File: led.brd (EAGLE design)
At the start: 60.9 x 55.9 mm, 12 parts

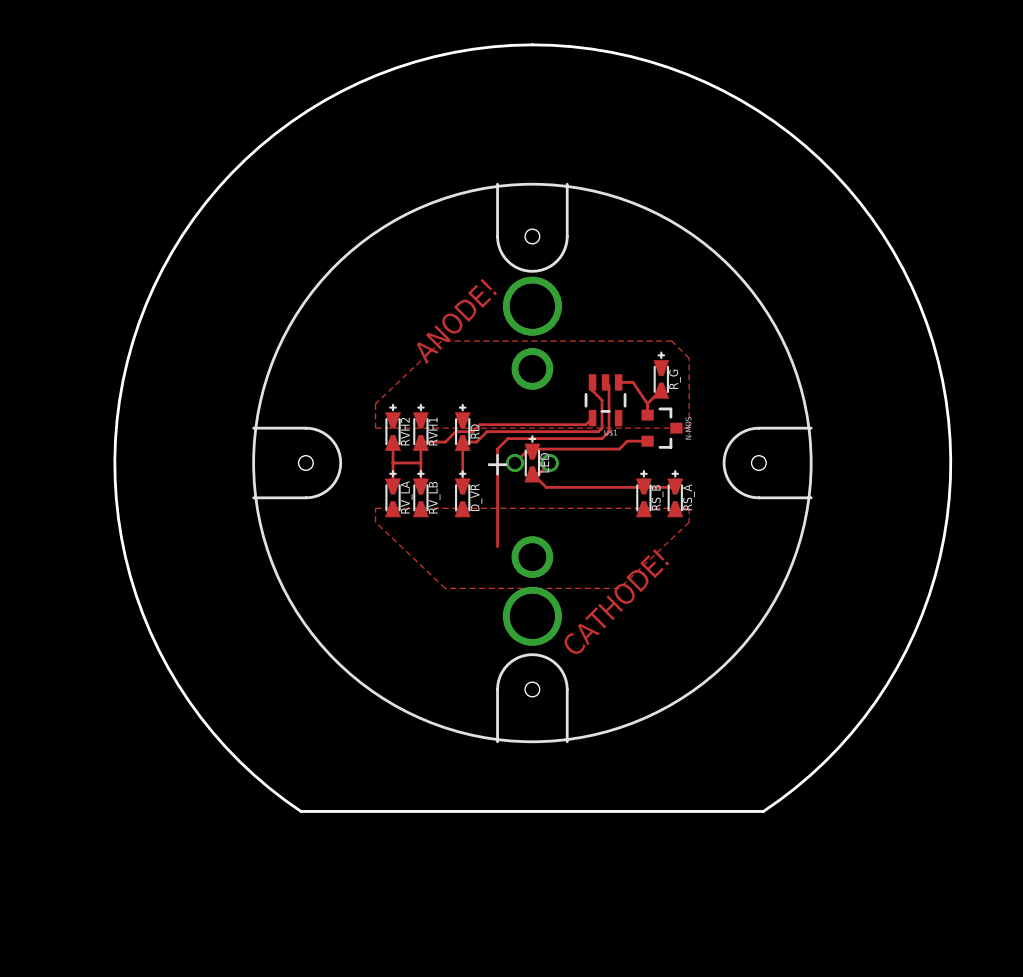
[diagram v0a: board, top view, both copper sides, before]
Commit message: correct LED circuit
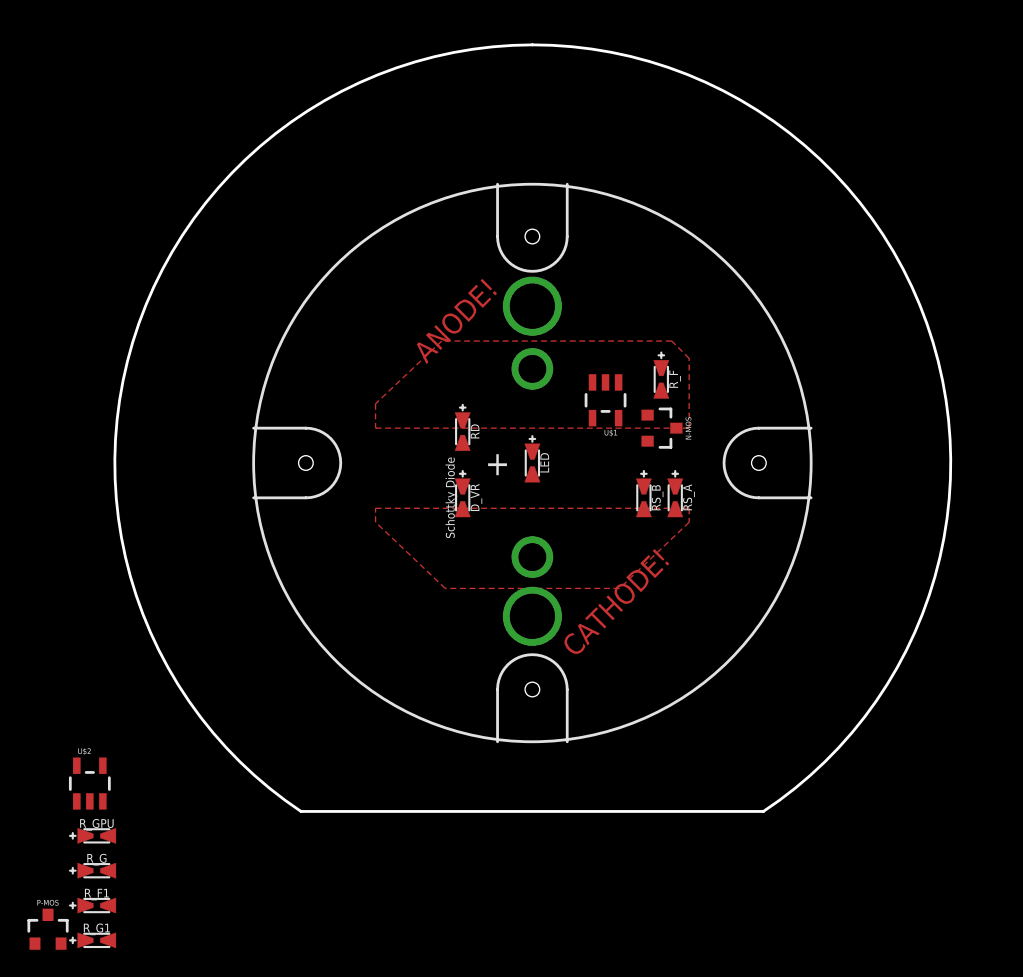
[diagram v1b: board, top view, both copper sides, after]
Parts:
- removed RVH1, RVH2, RV_LA, RV_LB: (no value), tekdemo:0402-0603-0805-UNIVERSAL
- added P-MOS: (no value), tekdemo:SOT23-3
- added R_F, R_F1, R_G1, R_GPU: (no value), tekdemo:0402-0603-0805-UNIVERSAL
- added U$2: OPA344, SparkFun-AnalogIC:SOT23-5
- D_VR: value (none) -> Schottky Diode
- moved R_G 54.6 mm to (-1.27, 0.76), turned to 0 degrees
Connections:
- removed net LED+: LED.+, N-MOS.2
- removed net LED-: LED.-, RS_A.+, RS_B.+
- removed net N$7: RVH1.-, RVH2.-, RV_LA.+, RV_LB.+, U$1.4
- removed net N$8: D_VR.+, RD.-, U$1.3
- new net GATE: N-MOS.1, R_GPU.+, U$2.1
- new net N$2: N-MOS.2, RS_A.+, RS_B.+
- new net VCC: LED.+, P-MOS.2, R_GPU.-, U$1.5, U$2.5
- new net VDIV: R_F.+, R_F1.+, R_G.-, R_G1.-, U$1.4
- new net VREF: RD.+, U$2.3
- new net VSENSE: LED.-, N-MOS.3, U$1.3
- new net V_AMP: R_F.-, R_F1.-, U$1.1, U$2.4
- net GND: now also P-MOS.1, R_G.+, R_G1.+, U$2.2; no longer RV_LA.-, RV_LB.-
- net N$3: now also D_VR.+, RD.-; no longer N-MOS.1, R_G.-, U$1.1
- net VIN: now also P-MOS.3; no longer N-MOS.3, RD.+, RVH1.+, RVH2.+, R_G.+, U$1.5
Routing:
- net N$7: track 21.9 -> 0.00 mm
- net GND: track 19.5 -> 0.00 mm
- net N$8: track 17.5 -> 0.00 mm
- net LED-: track 12.4 -> 0.00 mm, vias 1 -> 0
- net LED+: track 10.3 -> 0.00 mm, vias 1 -> 0
- net N$3: track 6.02 -> 0.00 mm

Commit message: routed led board
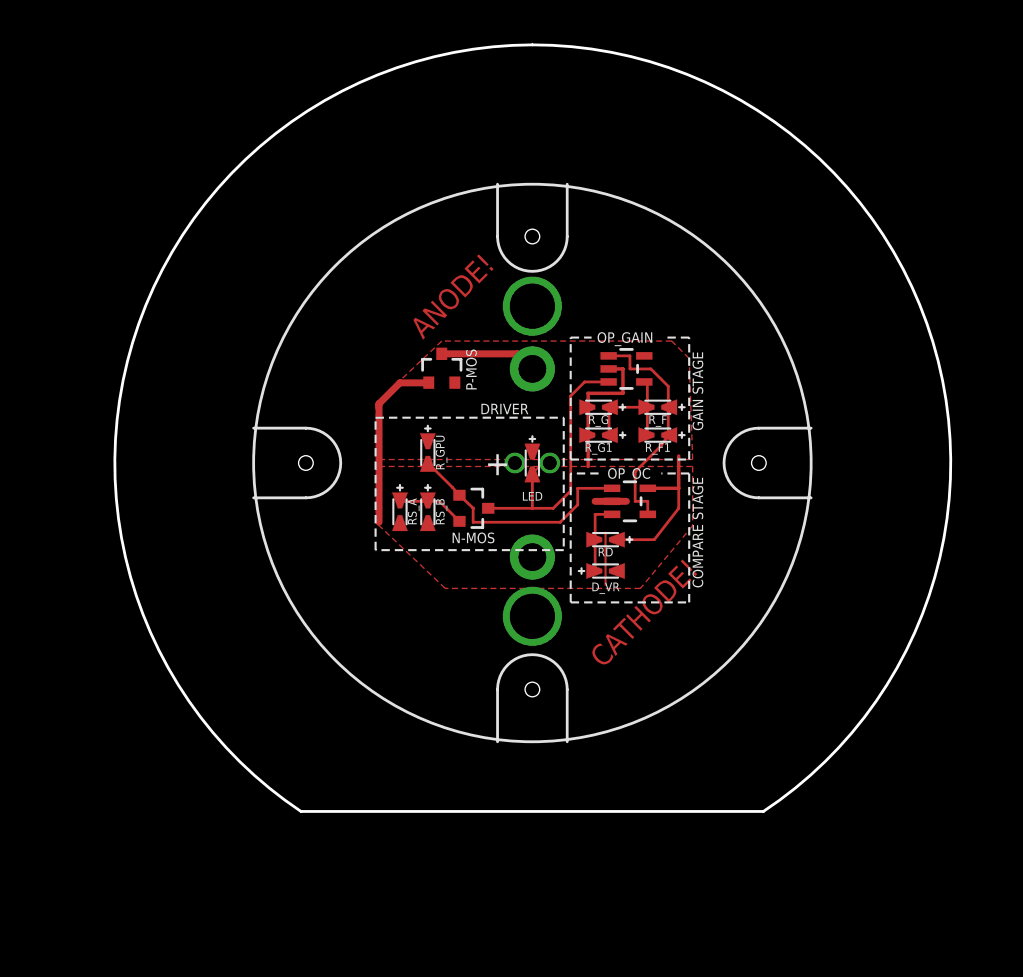
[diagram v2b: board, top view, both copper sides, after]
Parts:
- removed U$1, U$2: OPA344, SparkFun-AnalogIC:SOT23-5
- added OP_GAIN: (no value), SparkFun-AnalogIC:SOT23-5
- added OP_OC: OPA344, SparkFun-AnalogIC:SOT23-5
- D_VR: value Schottky Diode -> (none)
- moved R_F1 53.4 mm to (39.6, 32.5), turned to 180 degrees
- moved R_G1 51.9 mm to (35.3, 32.5), turned to 180 degrees
- moved P-MOS 50.0 mm to (23.9, 37.3)
- moved R_G 49.8 mm to (35.3, 34.5), turned to 180 degrees
- moved R_GPU 36.9 mm to (22.9, 31.2), turned to 270 degrees
- moved RS_A 20.1 mm to (20.8, 26.9)
- moved RS_B 15.8 mm to (22.9, 26.9)
- moved N-MOS 14.9 mm to (26.2, 27.2)
- moved RD 13.1 mm to (35.8, 24.9), turned to 180 degrees
- moved D_VR 11.7 mm to (35.8, 22.6), turned to 0 degrees
- moved R_F 2.05 mm to (39.6, 34.5), turned to 180 degrees
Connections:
- removed net N$3: D_VR.+, RD.-
- net GATE: now also OP_OC.1, R_GPU.-; no longer R_GPU.+, U$2.1
- net GND: now also OP_GAIN.2, OP_OC.2, R_G.-, R_G1.-; no longer R_G.+, R_G1.+, U$1.2, U$2.2
- net VCC: now also OP_GAIN.5, OP_OC.5, RD.+, R_GPU.+; no longer R_GPU.-, U$1.5, U$2.5
- net VDIV: now also OP_GAIN.4, R_F.-, R_F1.-, R_G.+, R_G1.+; no longer R_F.+, R_F1.+, R_G.-, R_G1.-, U$1.4
- net VREF: now also D_VR.+, OP_OC.3, RD.-; no longer RD.+, U$2.3
- net VSENSE: now also OP_GAIN.3; no longer U$1.3
- net V_AMP: now also OP_GAIN.1, OP_OC.4, R_F.+, R_F1.+; no longer R_F.-, R_F1.-, U$1.1, U$2.4
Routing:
- net GND: track 0.00 -> 29.7 mm
- net VSENSE: track 0.00 -> 20.8 mm, vias 0 -> 1
- net GATE: track 0.00 -> 17.6 mm
- net V_AMP: track 0.00 -> 17.0 mm
- net VCC: track 0.00 -> 11.8 mm, vias 0 -> 1
- net VDIV: track 0.00 -> 8.93 mm
- net VIN: track 0.00 -> 7.06 mm
- net VREF: track 0.00 -> 5.37 mm
- net N$2: track 0.00 -> 4.94 mm
- added copper zone on layer 1, net VCC
- removed copper zone on layer 1, net VIN
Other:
- board text added: "COMPARE STAGE"
- board text added: "DRIVER"
- board text added: "GAIN STAGE"

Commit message: confirm footprints and finalize for maker faire
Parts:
- added CAP_PB, CAP_PB1: 0.1uf, tekdemo:0402-0603-0805-UNIVERSAL
- RD, R_GPU: value (none) -> 10k
- RS_A: value (none) -> 1ohm
- RS_B: value (none) -> NONE
- R_F: value (none) -> 9-10k
- R_G: value (none) -> 1kohm
- moved R_GPU 2.55 mm to (25.4, 31.0)
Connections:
- net GND: now also CAP_PB.-, CAP_PB1.-, OP_GAIN.5, OP_OC.5; no longer OP_GAIN.2, OP_OC.2
- net VCC: now also CAP_PB.+, CAP_PB1.+, OP_GAIN.2, OP_OC.2; no longer OP_GAIN.5, OP_OC.5
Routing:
- net VCC: track 11.8 -> 13.3 mm
- net GATE: track 17.6 -> 16.4 mm
- net V_AMP: track 17.0 -> 17.8 mm
- net GND: track 29.7 -> 30.2 mm, vias 1 -> 2
- added copper zone on layer 16, net GND
- added copper zone on layer 1, net N$5
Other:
- board size 60.9 x 55.9 mm -> 58.9 x 53.6 mm

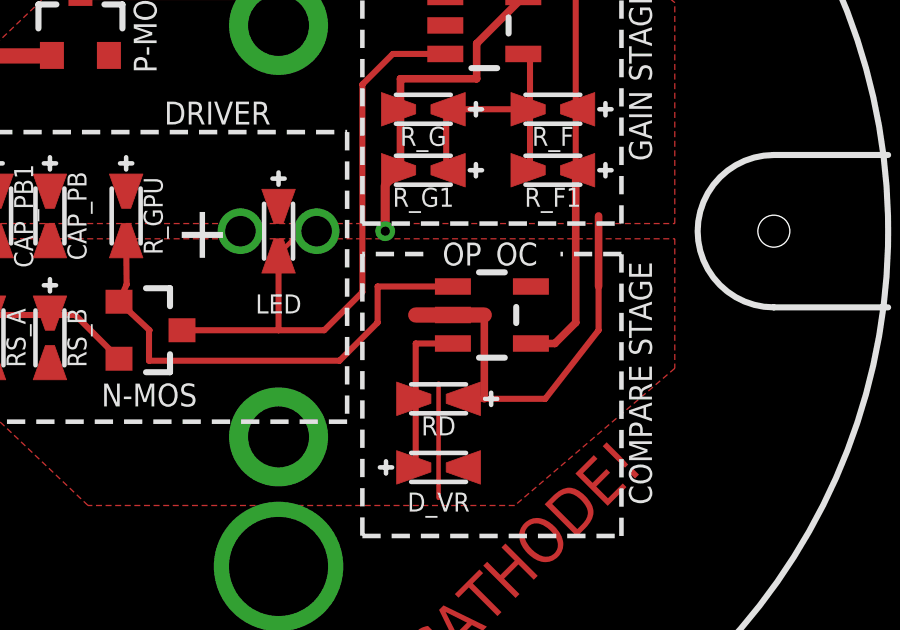
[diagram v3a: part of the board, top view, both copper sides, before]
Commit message: Removed short caused by old bad footprint
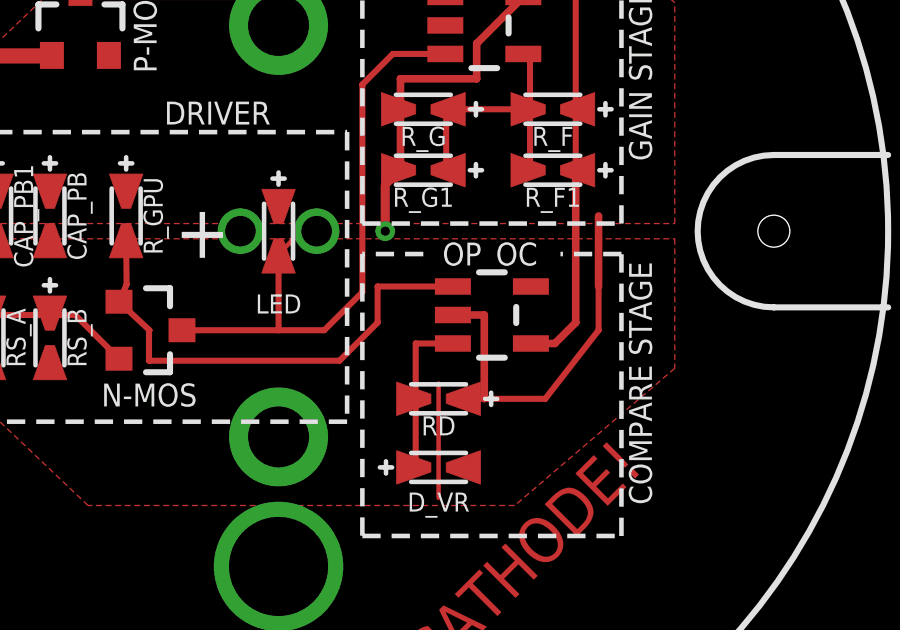
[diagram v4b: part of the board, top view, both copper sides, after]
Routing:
- net GND: track 30.2 -> 27.9 mm
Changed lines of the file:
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@@
 <grid distance="10" unitdist="mil" unit="mil" style="lines" multiple="5" display="yes" altdistance="1" altunitdist="mil" altunit="mil"/>
 <layers>
-<layer number="1" name="Top" color="4" fill="7" visible="no" active="yes"/>
+<layer number="1" name="Top" color="4" fill="7" visible="yes" active="yes"/>
 <layer number="16" name="Bottom" color="1" fill="11" visible="no" active="yes"/>
 <layer number="17" name="Pads" color="2" fill="1" visible="yes" active="yes"/>
@@
 <layer number="19" name="Unrouted" color="6" fill="1" visible="yes" active="yes"/>
 <layer number="20" name="Dimension" color="15" fill="1" visible="yes" active="yes"/>
-<layer number="21" name="tPlace" color="16" fill="1" visible="no" active="yes"/>
-<layer number="22" name="bPlace" color="14" fill="1" visible="yes" active="yes"/>
-<layer number="23" name="tOrigins" color="15" fill="1" visible="no" active="yes"/>
+<layer number="21" name="tPlace" color="16" fill="1" visible="yes" active="yes"/>
+<layer number="22" name="bPlace" color="14" fill="1" visible="no" active="yes"/>
+<layer number="23" name="tOrigins" color="15" fill="1" visible="yes" active="yes"/>
 <layer number="24" name="bOrigins" color="15" fill="1" visible="yes" active="yes"/>
 <layer number="25" name="tNames" color="7" fill="1" visible="no" active="yes"/>
@@
 <layer number="27" name="tValues" color="7" fill="1" visible="no" active="yes"/>
 <layer number="28" name="bValues" color="7" fill="1" visible="no" active="yes"/>
-<layer number="29" name="tStop" color="7" fill="3" visible="no" active="yes"/>
+<layer number="29" name="tStop" color="7" fill="3" visible="yes" active="yes"/>
 <layer number="30" name="bStop" color="7" fill="6" visible="yes" active="yes"/>
 <layer number="31" name="tCream" color="7" fill="4" visible="no" active="yes"/>
@@
 <wire x1="20.828" y1="36.322" x2="19.304" y2="34.798" width="0.508" layer="1"/>
 <wire x1="19.304" y1="34.798" x2="19.304" y2="26.162" width="0.508" layer="1"/>
-<wire x1="37.338" y1="27.686" x2="35.052" y2="27.686" width="0.508" layer="1"/>
 <wire x1="35.814" y1="25.4" x2="35.814" y2="21.59" width="0.1524" layer="1"/>
 <contactref element="OP_GAIN" pad="5"/>
